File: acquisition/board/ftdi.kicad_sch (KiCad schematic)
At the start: 48 parts, among them J18 UX60SX-MB-5ST, U10 FT232HL, U18 74AVCH1T45, U21 ECS-3225MVQ-120-CN-TR, U22 93LC56B-MS, U29 SIP32408, U6 ICE40UP5K_QFN48

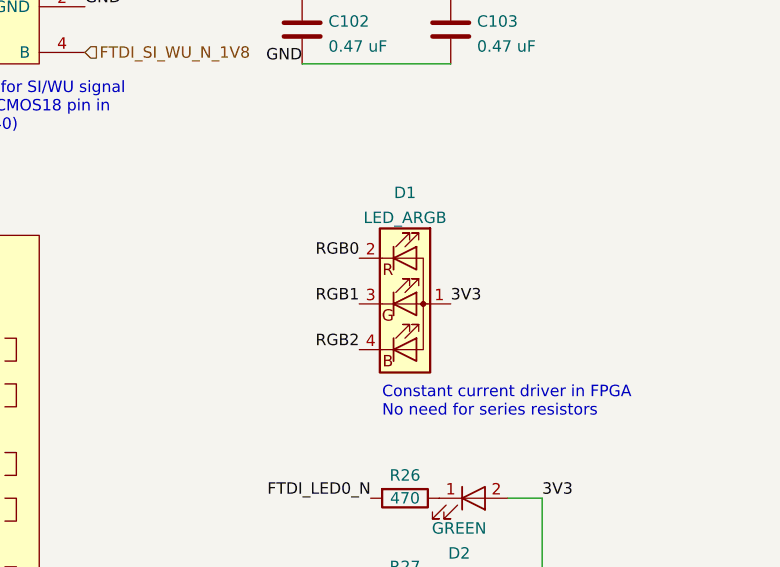
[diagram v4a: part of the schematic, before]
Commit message: Finished footprint assignment
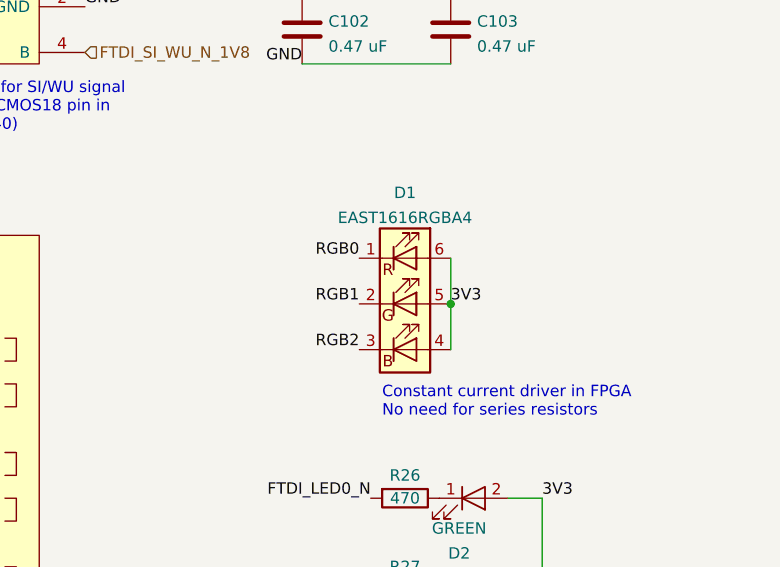
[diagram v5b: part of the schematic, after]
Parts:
- removed D1: LED_ARGB, symbol device:LED_ARGB
- added D1: EAST1616RGBA4, azonenberg_pcb:LED_EVERLIGHT_EAST1616RGBA4, symbol device:LED_RGB
- D2, D3: footprint (none) -> azonenberg_pcb:EIA_0603_LED
- D25, D26, D27: footprint (none) -> azonenberg_pcb:DFN_2_1x0.6_TI_DPY
- L3, L4, L5: footprint (none) -> azonenberg_pcb:EIA_0603_INDUCTOR_NOSILK
- U10: footprint (none) -> azonenberg_pcb:QFP_48_0.5MM
- U18: footprint (none) -> azonenberg_pcb:DFN_6_0.5MM_1.45x1.00MM
- U21: footprint (none) -> azonenberg_pcb:OSCILLATOR_3.2x2.5
- U22: footprint (none) -> azonenberg_pcb:SOP_8_0.5MM_3MM
- U29: footprint (none) -> azonenberg_pcb:DFN_4_0.5MM_1.6x1.2MM
- U6: footprint (none) -> azonenberg_pcb:QFN_48_0.5MM_7x7MM
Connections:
- net 3V3: now also D1.4 (BA), D1.5 (GA), D1.6 (RA)
- net RGB0: now also D1.1 (RK)
- net RGB1: now also D1.2 (GK)
- net RGB2: now also D1.3 (BK)
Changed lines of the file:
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@@
   (title_block
     (title "Digitizer board")
-    (date "2022-07-17")
+    (date "2023-01-29")
     (rev "0.1")
     (company "A. Zonenberg")
@@
   )
   (junction (at 114.3 175.26) (diameter 0) (color 0 0 0 0)
+  )
+  (junction (at 248.92 57.15) (diameter 0) (color 0 0 0 0)
   )
   (junction (at 66.04 20.32) (diameter 0) (color 0 0 0 0)
@@
     (stroke (width 0) (type default) (color 0 0 0 0))
   )
+  (wire (pts (xy 248.92 57.15) (xy 248.92 62.23))
+    (stroke (width 0) (type default) (color 0 0 0 0))
+  )
   (wire (pts (xy 78.74 151.13) (xy 91.44 151.13))
     (stroke (width 0) (type default) (color 0 0 0 0))
@@
   )
   (wire (pts (xy 111.76 121.92) (xy 114.3 121.92))
+    (stroke (width 0) (type default) (color 0 0 0 0))
+  )
+  (wire (pts (xy 248.92 52.07) (xy 248.92 57.15))
     (stroke (width 0) (type default) (color 0 0 0 0))
   )
@@
     (property "Reference" "D2" (id 0) (at 249.8598 84.8655 0))
     (property "Value" "GREEN" (id 1) (at 249.8598 82.0904 0))
-    (property "Footprint" "" (id 2) (at 251.46 78.74 0)
+    (property "Footprint" "azonenberg_pcb:EIA_0603_LED" (id 2) (at 251.46 78.74 0)
       (effects (font (size 1.27 1.27)) hide)
     )
@@
       (effects (font (size 1.524 1.524)))
     )
-    (property "Footprint" "" (id 2) (at 212.09 139.7 0)
+    (property "Footprint" "azonenberg_pcb:SOP_8_0.5MM_3MM" (id 2) (at 212.09 139.7 0)
       (effects (font (size 1.524 1.524)) hide)
     )
@@
       (effects (font (size 1.27 1.27)) (justify left))
     )
-    (property "Footprint" "" (id 2) (at 186.69 95.25 0)
+    (property "Footprint" "azonenberg_pcb:QFN_48_0.5MM_7x7MM" (id 2) (at 186.69 95.25 0)
       (effects (font (size 1.27 1.27)) hide)
     )
@@
       (effects (font (size 1.27 1.27)) (justify right))
     )
-    (property "Footprint" "" (id 2) (at 31.75 55.88 0)
+    (property "Footprint" "azonenberg_pcb:DFN_2_1x0.6_TI_DPY" (id 2) (at 31.75 55.88 0)
       (effects (font (size 1.27 1.27)) hide)
     )
@@
       (effects (font (size 1.27 1.27)) (justify right))
     )
-    (property "Footprint" "" (id 2) (at 31.75 68.58 0)
+    (property "Footprint" "azonenberg_pcb:DFN_2_1x0.6_TI_DPY" (id 2) (at 31.75 68.58 0)
       (effects (font (size 1.27 1.27)) hide)
     )
@@
       (effects (font (size 1.016 1.016)))
     )
-    (property "Footprint" "" (id 2) (at 58.42 20.32 0)
+    (property "Footprint" "azonenberg_pcb:EIA_0603_INDUCTOR_NOSILK" (id 2) (at 58.42 20.32 0)
       (effects (font (size 1.524 1.524)) hide)
     )
@@
       (effects (font (size 1.524 1.524)))
     )
-    (property "Footprint" "" (id 2) (at 186.69 30.48 0)
+    (property "Footprint" "azonenberg_pcb:DFN_6_0.5MM_1.45x1.00MM" (id 2) (at 186.69 30.48 0)
       (effects (font (size 1.524 1.524)) hide)
     )
@@
       (effects (font (size 1.524 1.524)))
     )
-    (property "Footprint" "" (id 2) (at 82.55 34.29 0)
+    (property "Footprint" "azonenberg_pcb:DFN_4_0.5MM_1.6x1.2MM" (id 2) (at 82.55 34.29 0)
       (effects (font (size 1.524 1.524)) hide)
     )
@@
       (effects (font (size 1.27 1.27)) (justify right))
     )
-    (property "Footprint" "" (id 2) (at 31.75 44.45 0)
+    (property "Footprint" "azonenberg_pcb:DFN_2_1x0.6_TI_DPY" (id 2) (at 31.75 44.45 0)
       (effects (font (size 1.27 1.27)) hide)
     )
@@
       (effects (font (size 1.016 1.016)))
     )
-    (property "Footprint" "" (id 2) (at 71.12 163.83 0)
+    (property "Footprint" "azonenberg_pcb:EIA_0603_INDUCTOR_NOSILK" (id 2) (at 71.12 163.83 0)
       (effects (font (size 1.524 1.524)) hide)
     )
@@
     (pin "1")
     (pin "2")
+  )
+  (symbol (lib_id "device:LED_RGB") (at 243.84 57.15 0) (unit 1)
+    (in_bom yes) (on_board yes) (fields_autoplaced)
+    (property "Reference" "D1" (id 0) (at 243.84 44.8015 0))
+    (property "Value" "EAST1616RGBA4" (id 1) (at 243.84 47.5766 0))
+    (property "Footprint" "azonenberg_pcb:LED_EVERLIGHT_EAST1616RGBA4" (id 2) (at 243.84 58.42 0)
+      (effects (font (size 1.27 1.27)) hide)
+    )
+    (property "Datasheet" "" (id 3) (at 243.84 58.42 0)
+      (effects (font (size 1.27 1.27)) hide)
+    )
+    (pin "1")
+    (pin "2")
+    (pin "3")
+    (pin "4")
+    (pin "5")
+    (pin "6")
   )
   (symbol (lib_id "passive-azonenberg:INDUCTOR_PWROUT") (at 71.12 151.13 270) (unit 1)
@@
       (effects (font (size 1.016 1.016)))
     )
-    (property "Footprint" "" (id 2) (at 71.12 151.13 0)
+    (property "Footprint" "azonenberg_pcb:EIA_0603_INDUCTOR_NOSILK" (id 2) (at 71.12 151.13 0)
       (effects (font (size 1.524 1.524)) hide)
     )
@@
     (property "Reference" "D3" (id 0) (at 251.46 95.25 0))
     (property "Value" "GREEN" (id 1) (at 251.46 92.71 0))
-    (property "Footprint" "" (id 2) (at 251.46 88.9 0)
+    (property "Footprint" "azonenberg_pcb:EIA_0603_LED" (id 2) (at 251.46 88.9 0)
       (effects (font (size 1.27 1.27)) hide)
     )
@@
     (pin "2")
   )
-  (symbol (lib_id "device:LED_ARGB") (at 243.84 57.15 0) (unit 1)
-    (in_bom yes) (on_board yes) (fields_autoplaced)
-    (property "Reference" "D1" (id 0) (at 243.84 44.8015 0))
-    (property "Value" "LED_ARGB" (id 1) (at 243.84 47.5766 0))
-    (property "Footprint" "" (id 2) (at 243.84 58.42 0)
-      (effects (font (size 1.27 1.27)) hide)
-    )
-    (property "Datasheet" "" (id 3) (at 243.84 58.42 0)
-      (effects (font (size 1.27 1.27)) hide)
+  (symbol (lib_id "osc-azonenberg:OSC") (at 44.45 104.14 0) (unit 1)
+    (in_bom yes) (on_board yes) (fields_autoplaced)
+    (property "Reference" "U21" (id 0) (at 43.815 97.1961 0)
+      (effects (font (size 1.524 1.524)))
+    )
+    (property "Value" "ECS-3225MVQ-120-CN-TR" (id 1) (at 43.815 100.4751 0)
+      (effects (font (size 1.524 1.524)))
+    )
+    (property "Footprint" "azonenberg_pcb:OSCILLATOR_3.2x2.5" (id 2) (at 44.45 104.14 0)
+      (effects (font (size 1.524 1.524)) hide)
+    )
+    (property "Datasheet" "" (id 3) (at 44.45 104.14 0)
+      (effects (font (size 1.524 1.524)))
     )
     (pin "1")
@@
     (pin "4")
   )
-  (symbol (lib_id "osc-azonenberg:OSC") (at 44.45 104.14 0) (unit 1)
-    (in_bom yes) (on_board yes) (fields_autoplaced)
-    (property "Reference" "U21" (id 0) (at 43.815 97.1961 0)
-      (effects (font (size 1.524 1.524)))
-    )
-    (property "Value" "ECS-3225MVQ-120-CN-TR" (id 1) (at 43.815 100.4751 0)
-      (effects (font (size 1.524 1.524)))
-    )
-    (property "Footprint" "" (id 2) (at 44.45 104.14 0)
-      (effects (font (size 1.524 1.524)) hide)
-    )
-    (property "Datasheet" "" (id 3) (at 44.45 104.14 0)
-      (effects (font (size 1.524 1.524)))
-    )
-    (pin "1")
-    (pin "2")
-    (pin "3")
-    (pin "4")
-  )
   (symbol (lib_id "device:C") (at 248.92 26.67 0) (unit 1)
     (in_bom yes) (on_board yes) (fields_autoplaced)
@@
       (effects (font (size 1.524 1.524)) (justify left))
     )
-    (property "Footprint" "" (id 2) (at 109.22 86.36 0)
+    (property "Footprint" "azonenberg_pcb:QFP_48_0.5MM" (id 2) (at 109.22 86.36 0)
       (effects (font (size 1.524 1.524)) hide)
     )
